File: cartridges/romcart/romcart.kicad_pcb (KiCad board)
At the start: 2 copper layers, 72 x 51.8 mm, 7 parts, among them J1 Proto Connector, SW1 SW_SPDT, U1 27C512, U2 SG-1000-Cart

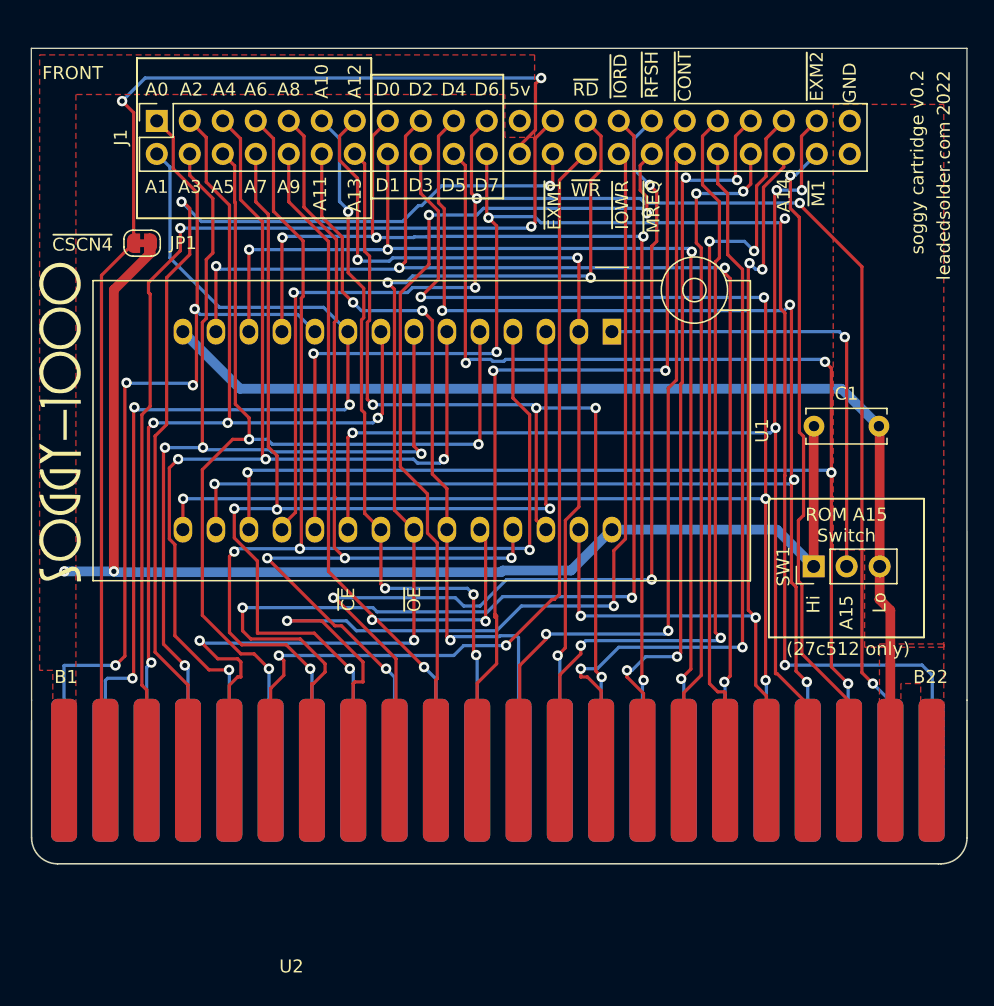
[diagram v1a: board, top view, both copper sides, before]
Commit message: Carts to KiCad 7
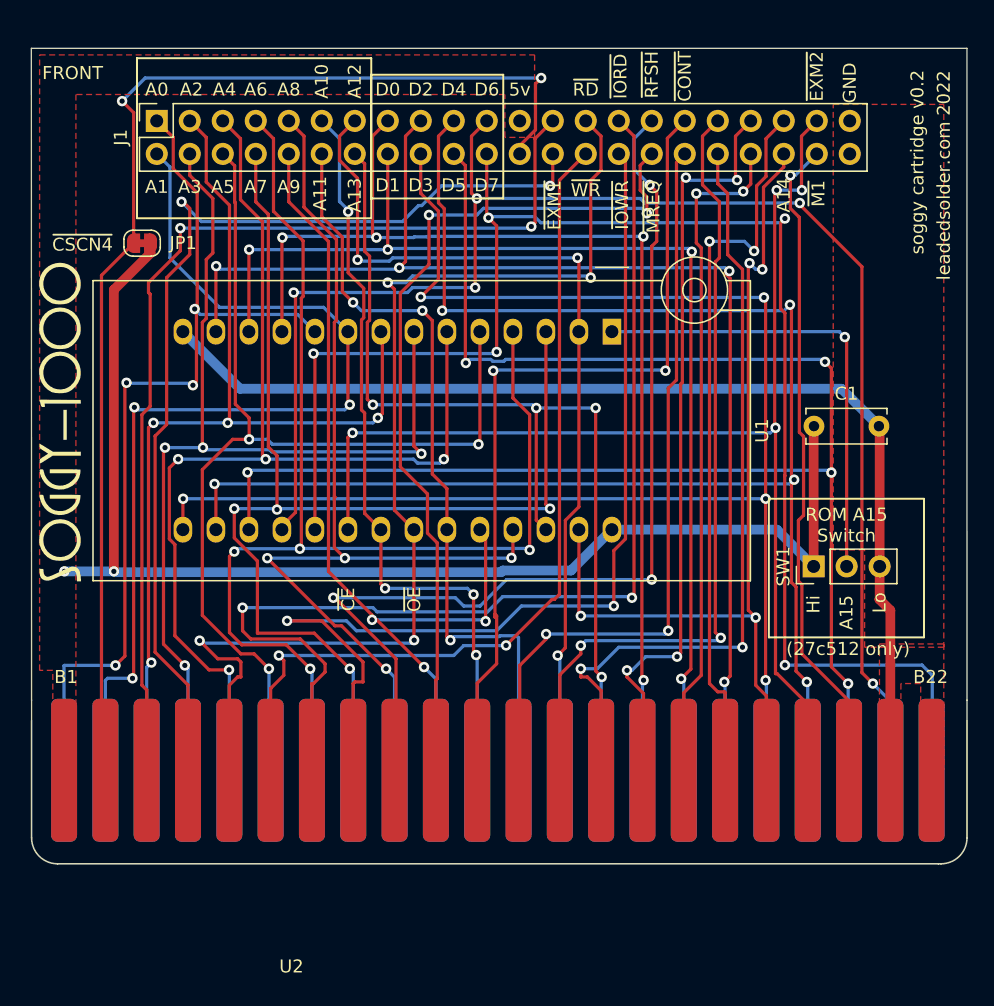
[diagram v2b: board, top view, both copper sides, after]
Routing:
- net /~{RCSEL}: track 61.9 -> 56.2 mm
